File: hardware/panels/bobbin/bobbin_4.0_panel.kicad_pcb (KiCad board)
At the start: 2 copper layers, 90.5 x 105 mm, 34 parts

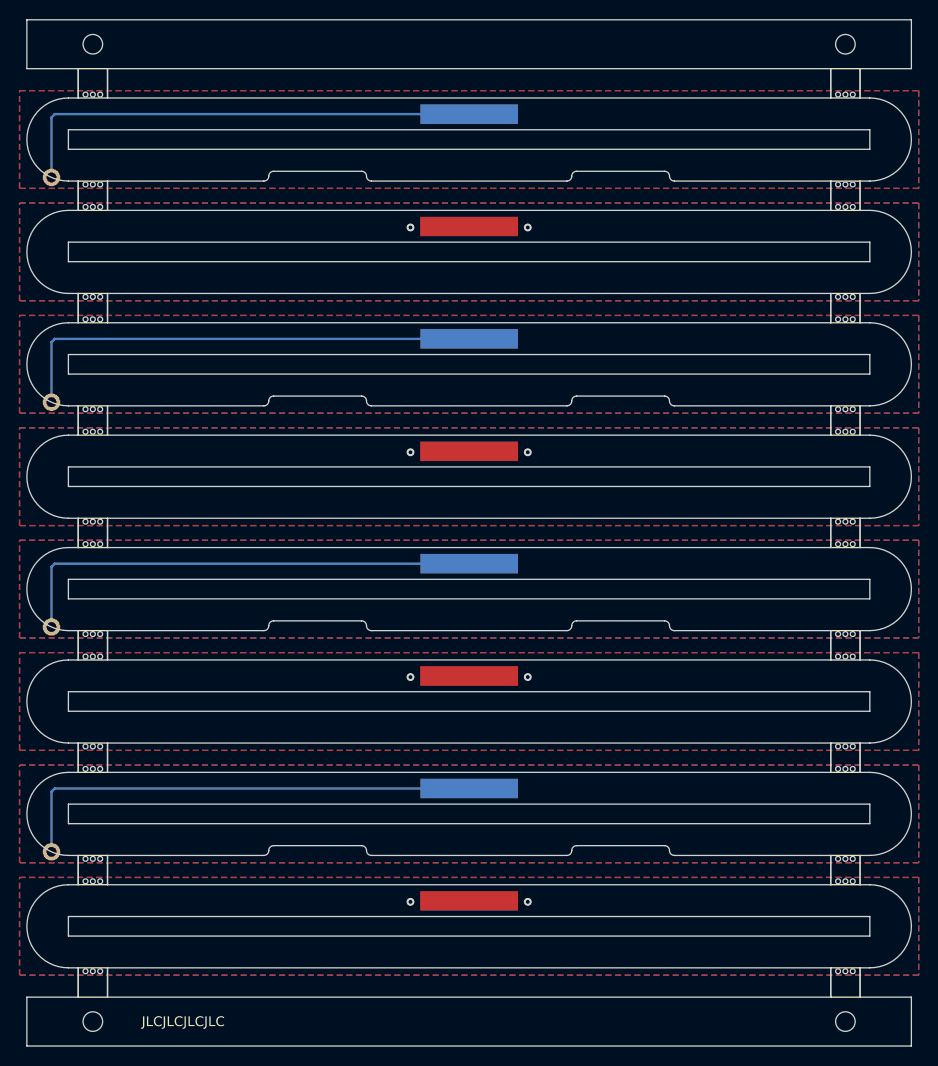
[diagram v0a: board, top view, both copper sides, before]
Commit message: Preamp, Tone Block, Passive, and Bobbin Panel updates
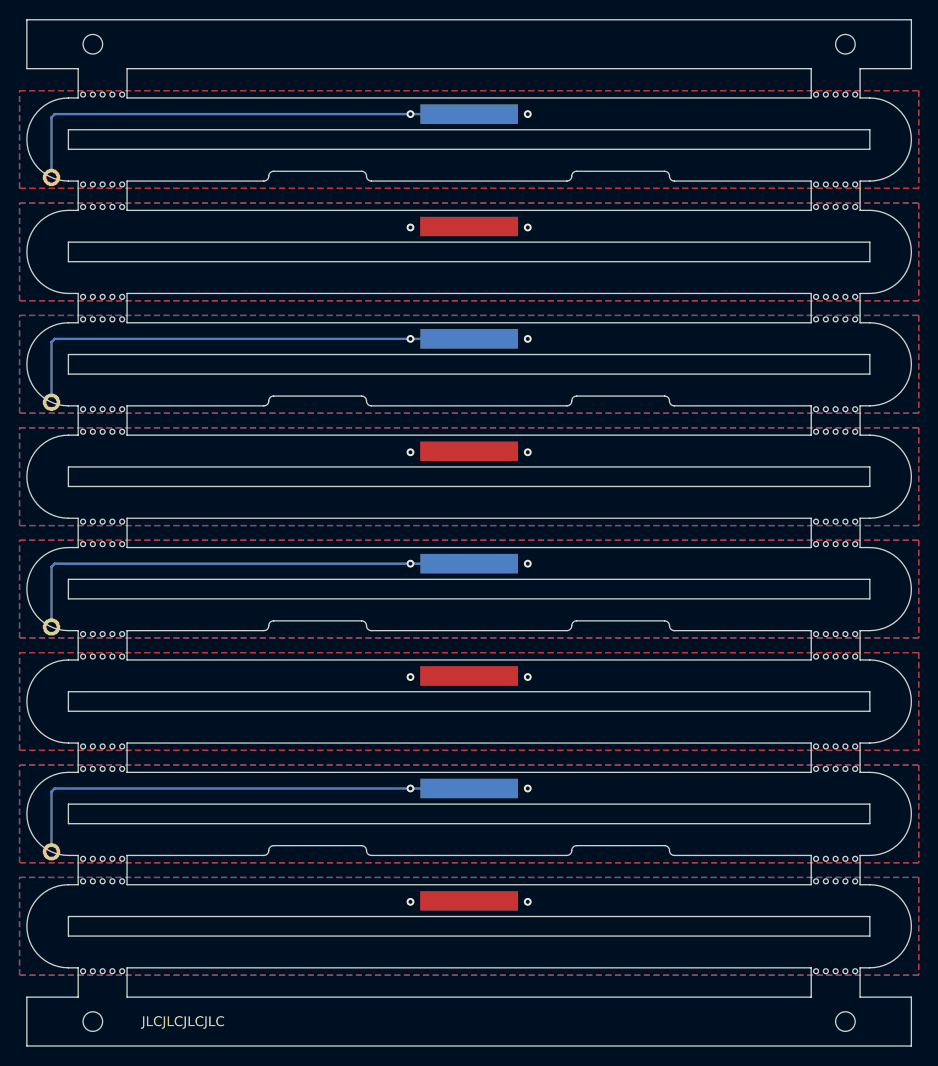
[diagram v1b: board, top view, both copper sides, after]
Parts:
- moved mouse-bite-3mm-slot 1.00 mm to (49.0, 131.0)
- moved mouse-bite-3mm-slot 1.00 mm to (124.0, 73.5)
- moved mouse-bite-3mm-slot 1.00 mm to (124.0, 108.0)
- moved mouse-bite-3mm-slot 1.00 mm to (124.0, 85.0)
- moved mouse-bite-3mm-slot 1.00 mm to (49.0, 108.0)
- moved mouse-bite-3mm-slot 1.00 mm to (49.0, 85.0)
- moved mouse-bite-3mm-slot 1.00 mm to (124.0, 62.0)
- moved mouse-bite-3mm-slot 1.00 mm to (49.0, 62.0)
- moved mouse-bite-3mm-slot 1.00 mm to (124.0, 50.5)
- moved mouse-bite-3mm-slot 1.00 mm to (49.0, 50.5)
- moved mouse-bite-3mm-slot 1.00 mm to (124.0, 131.0)
- moved mouse-bite-3mm-slot 1.00 mm to (124.0, 39.0)
- moved mouse-bite-3mm-slot 1.00 mm to (49.0, 39.0)
- moved mouse-bite-3mm-slot 1.00 mm to (49.0, 119.5)
- moved mouse-bite-3mm-slot 1.00 mm to (49.0, 96.5)
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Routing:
- net GND: vias 8 -> 16
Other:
- outline, holes or cut-outs redrawn
